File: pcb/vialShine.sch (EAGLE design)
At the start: 5 parts

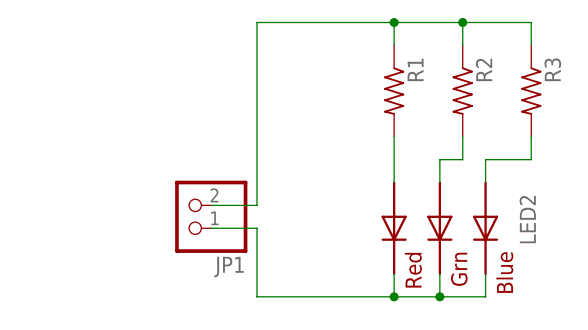
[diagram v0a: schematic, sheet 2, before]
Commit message: Added simple 5050 LED and resistors.
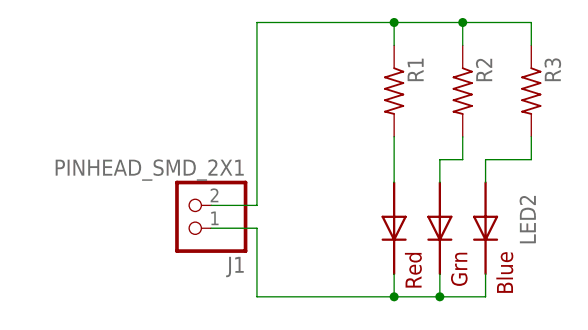
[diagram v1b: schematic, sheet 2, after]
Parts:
- removed JP1: (no value), pinhead:PINHD-1X2
- added J1: PINHEAD_SMD_2X1, vialShine:PINHEAD_SMD_2X1
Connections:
- net N$2: now also J1.2; no longer JP1.2
- net N$3: now also J1.1; no longer JP1.1
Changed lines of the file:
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@@
 <part name="FRAME1" library="frames" deviceset="FRAME_B_L" device=""/>
 <part name="FRAME2" library="frames" deviceset="FRAME_B_L" device=""/>
-<part name="JP1" library="pinhead" deviceset="PINHD-1X2" device=""/>
 <part name="R1" library="rcl" deviceset="R-US_" device="R0603"/>
 <part name="R2" library="rcl" deviceset="R-US_" device="R0603"/>
 <part name="R3" library="rcl" deviceset="R-US_" device="R0603"/>
 <part name="LED2" library="adafruit" deviceset="RGBLED" device="5050"/>
+<part name="J1" library="vialShine" deviceset="PINHEAD_SMD_2X1" device=""/>
 </parts>
 <sheets>
@@
 <instance part="FRAME2" gate="G$1" x="0" y="0"/>
 <instance part="FRAME2" gate="G$2" x="325.12" y="0"/>
-<instance part="JP1" gate="G$1" x="96.52" y="208.28" rot="R180"/>
 <instance part="R1" gate="G$1" x="119.38" y="220.98" rot="R270"/>
 <instance part="R2" gate="G$1" x="127" y="220.98" rot="R270"/>
 <instance part="R3" gate="G$1" x="134.62" y="220.98" rot="R270"/>
 <instance part="LED2" gate="G$1" x="124.46" y="205.74" rot="R270"/>
+<instance part="J1" gate="G$1" x="96.52" y="208.28" rot="R180"/>
 </instances>
 <busses>
@@
 <wire x1="104.14" y1="228.6" x2="104.14" y2="208.28" width="0.1524" layer="91"/>
 <junction x="119.38" y="228.6"/>
-<pinref part="JP1" gate="G$1" pin="2"/>
 <wire x1="104.14" y1="208.28" x2="99.06" y2="208.28" width="0.1524" layer="91"/>
+<pinref part="J1" gate="G$1" pin="2"/>
 </segment>
 </net>
@@
 <wire x1="124.46" y1="200.66" x2="124.46" y2="198.12" width="0.1524" layer="91"/>
 <junction x="124.46" y="198.12"/>
-<pinref part="JP1" gate="G$1" pin="1"/>
 <wire x1="99.06" y1="205.74" x2="104.14" y2="205.74" width="0.1524" layer="91"/>
 <wire x1="104.14" y1="205.74" x2="104.14" y2="198.12" width="0.1524" layer="91"/>
 <wire x1="119.38" y1="198.12" x2="104.14" y2="198.12" width="0.1524" layer="91"/>
 <junction x="119.38" y="198.12"/>
+<pinref part="J1" gate="G$1" pin="1"/>
 </segment>
 </net>
